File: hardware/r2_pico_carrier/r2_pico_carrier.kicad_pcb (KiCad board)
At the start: 2 copper layers, 80 x 72 mm, 63 parts, among them J1 5V in, J2 OLED SSD1306, SW1 display, U1 PCA9517A

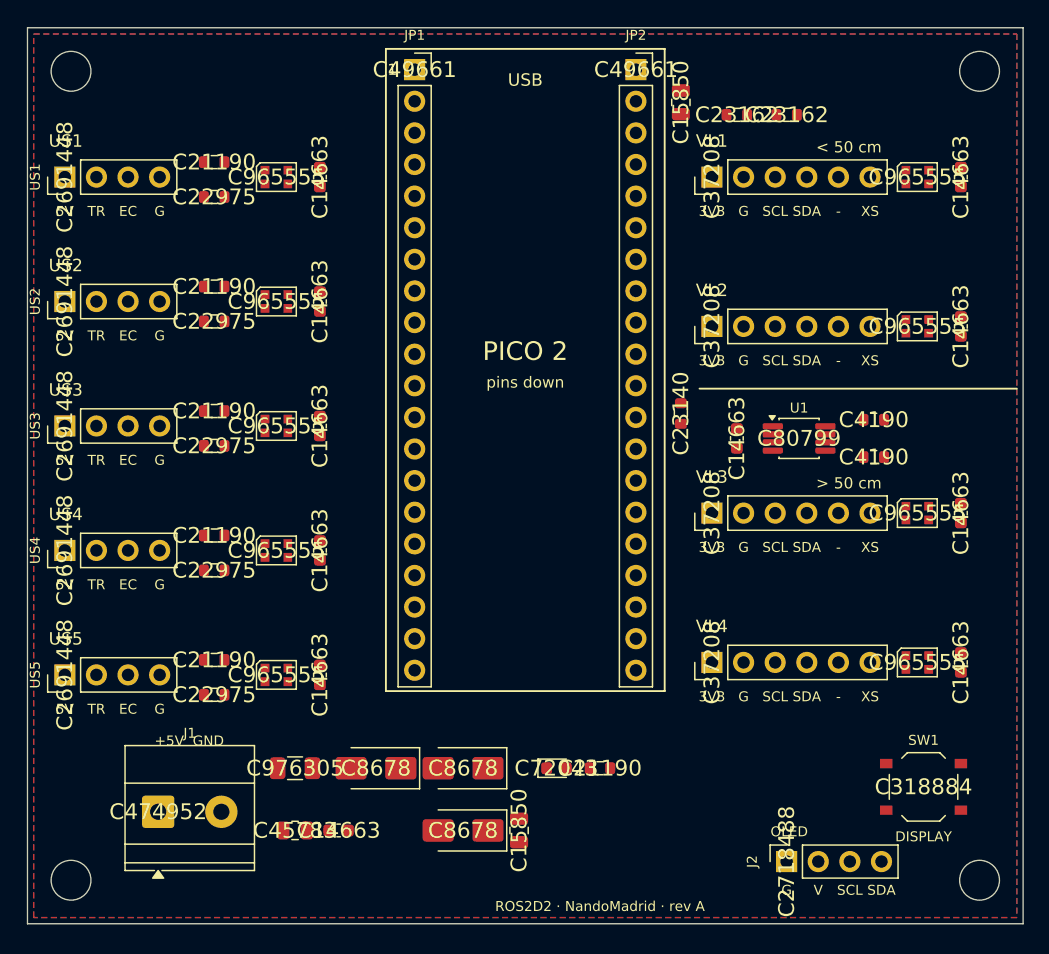
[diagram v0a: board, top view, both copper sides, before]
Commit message: Carrier board: routed, DRC and schematic parity clean
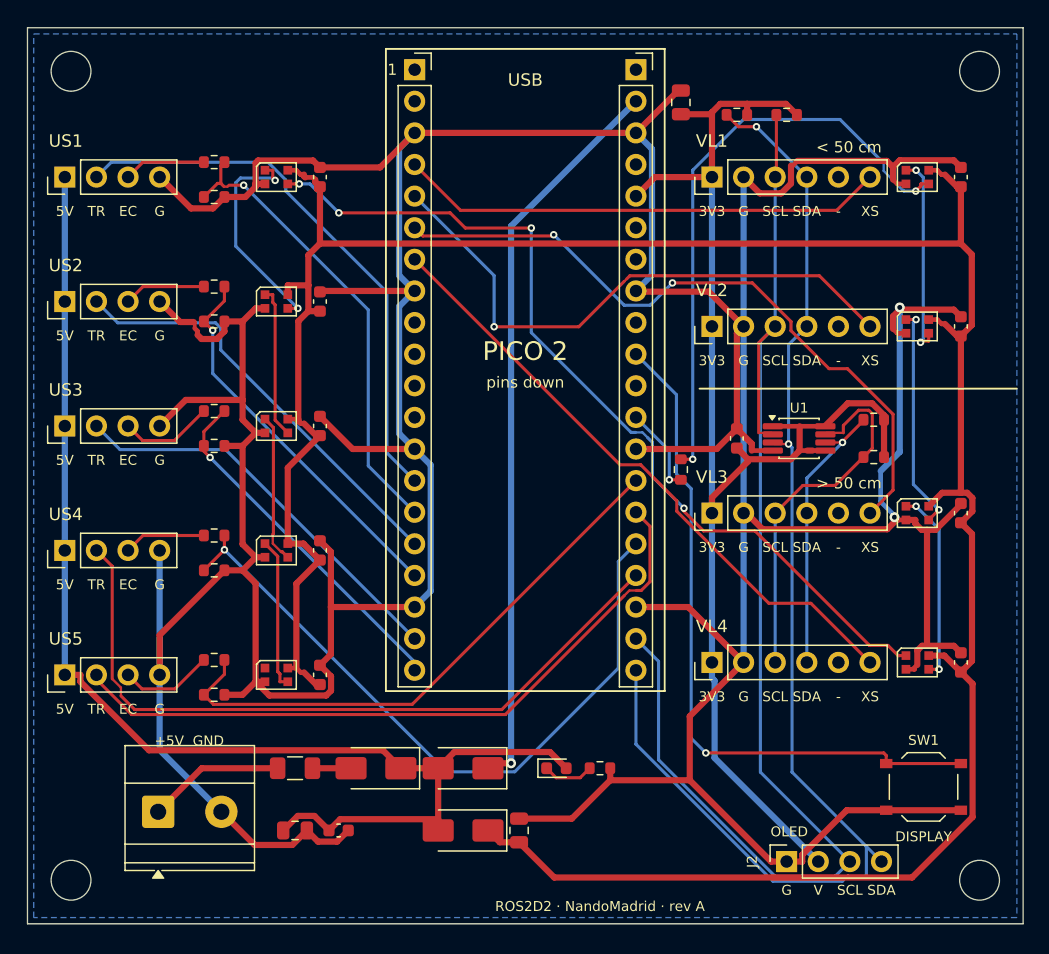
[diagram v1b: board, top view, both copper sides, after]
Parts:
- moved R6 4.50 mm to (52.5, 35.5)
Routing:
- net GND: track 0.00 -> 470.4 mm, vias 0 -> 2
- net VLED: track 0.00 -> 214.8 mm
- net +3V3: track 0.00 -> 110.1 mm
- net SCL: track 0.00 -> 104.0 mm
- net +5V: track 0.00 -> 103.6 mm
- net SDA: track 0.00 -> 100.1 mm, vias 0 -> 2
- net LED_D4: track 0.00 -> 72.1 mm, vias 0 -> 4
- net VSYS: track 0.00 -> 59.4 mm, vias 0 -> 1
- net TRIG4: track 0.00 -> 58.8 mm
- net ECHO4_P: track 0.00 -> 56.5 mm, vias 0 -> 1
- net TRIG5: track 0.00 -> 56.5 mm
- net BTN: track 0.00 -> 55.6 mm, vias 0 -> 1
- net XSHUT3: track 0.00 -> 55.4 mm, vias 0 -> 2
- net XSHUT4: track 0.00 -> 50.5 mm
- net LED_DIN: track 0.00 -> 47.9 mm, vias 0 -> 2
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- removed copper zone on F.Cu, net GND
